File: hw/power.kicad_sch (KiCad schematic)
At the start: 6 parts, among them Q1 SI2301CDS-T1-GE3, U7 XC6206P332MR

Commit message: hw: add more information to BOM
Signed-off-by: Mahyar Koshkouei <mk@deltabeard.com>
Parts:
- C21, C22: MFr (none) -> CL10A105KB8NNNC; Manufacturer (none) -> Samsung Electro-Mechanics; Notes (none) -> Alternative manufacturer is acceptable
- D1: Manufacturer (none) -> Changjiang Electronics Tech (CJ)
- Q1: MFr (none) -> SI2301CDS-T1-GE3; Manufacturer (none) -> Vishay Intertech
- R8: MFr (none) -> 0603WAF1003T5E; Manufacturer (none) -> UNI-ROYAL(Uniroyal Elec); Notes (none) -> Alternative manufacturer is acceptable
- U7: MFr (none) -> XC6206P332MR; Manufacturer (none) -> Torex Semicon
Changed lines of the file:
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@@
+      (effects (font (size 1.27 1.27)) hide)
+    )
+    (property "Notes" "Alternative manufacturer is acceptable" (id 5) (at 116.84 102.87 0)
+      (effects (font (size 1.27 1.27)) hide)
+    )
+    (property "Description" " ±1% 100kΩ ±100ppm/℃ 0.1W 0603 Chip Resistor - Surface Mount ROHS " (id 6) (at 116.84 102.87 0)
+      (effects (font (size 1.27 1.27)) hide)
+    )
+    (property "MFr" "0603WAF1003T5E" (id 7) (at 116.84 102.87 0)
+      (effects (font (size 1.27 1.27)) hide)
+    )
+    (property "Manufacturer" " UNI-ROYAL(Uniroyal Elec) " (id 8) (at 116.84 102.87 0)
       (effects (font (size 1.27 1.27)) hide)
     )
@@
       (effects (font (size 1.27 1.27)) hide)
     )
+    (property "Description" " X5R ±10% 50V 1uF 0603 Multilayer Ceramic Capacitors MLCC - SMD/SMT ROHS " (id 5) (at 154.94 81.28 0)
+      (effects (font (size 1.27 1.27)) hide)
+    )
+    (property "MFr" "CL10A105KB8NNNC" (id 6) (at 154.94 81.28 0)
+      (effects (font (size 1.27 1.27)) hide)
+    )
+    (property "Manufacturer" " Samsung Electro-Mechanics " (id 7) (at 154.94 81.28 0)
+      (effects (font (size 1.27 1.27)) hide)
+    )
+    (property "Notes" "Alternative manufacturer is acceptable" (id 8) (at 154.94 81.28 0)
+      (effects (font (size 1.27 1.27)) hide)
+    )
     (pin "1")
     (pin "2")
@@
       (effects (font (size 1.27 1.27)) hide)
     )
+    (property "Description" " X5R ±10% 50V 1uF 0603 Multilayer Ceramic Capacitors MLCC - SMD/SMT ROHS " (id 5) (at 181.61 81.28 0)
+      (effects (font (size 1.27 1.27)) hide)
+    )
+    (property "MFr" "CL10A105KB8NNNC" (id 6) (at 181.61 81.28 0)
+      (effects (font (size 1.27 1.27)) hide)
+    )
+    (property "Manufacturer" " Samsung Electro-Mechanics " (id 7) (at 181.61 81.28 0)
+      (effects (font (size 1.27 1.27)) hide)
+    )
+    (property "Notes" "Alternative manufacturer is acceptable" (id 8) (at 181.61 81.28 0)
+      (effects (font (size 1.27 1.27)) hide)
+    )
     (pin "1")
     (pin "2")
@@
     )
     (property "MFr" "BAV70" (id 5) (at 139.7 77.47 0)
+      (effects (font (size 1.27 1.27)) hide)
+    )
+    (property "Description" " +150℃ (Tj) 225mW 6ns 1.25V 150mA 200mA Dual Common Cathode 70V 2.5uA 70V SOT-23 Switching Diode ROHS " (id 6) (at 139.7 77.47 0)
+      (effects (font (size 1.27 1.27)) hide)
+    )
+    (property "Manufacturer" " Changjiang Electronics Tech (CJ) " (id 7) (at 139.7 77.47 0)
       (effects (font (size 1.27 1.27)) hide)
     )
@@
       (effects (font (size 1.27 1.27)) hide)
     )
+    (property "Description" " +150℃ (Tj) 225mW 6ns 1.25V 150mA 200mA Dual Common Cathode 70V 2.5uA 70V SOT-23 Switching Diode ROHS " (id 6) (at 139.7 88.9 0)
+      (effects (font (size 1.27 1.27)) hide)
+    )
+    (property "Manufacturer" " Changjiang Electronics Tech (CJ) " (id 7) (at 139.7 88.9 0)
+      (effects (font (size 1.27 1.27)) hide)
+    )
     (pin "2")
   )
@@
     )
     (property "LCSC" "C10487" (id 4) (at 124.46 91.44 0)
+      (effects (font (size 1.27 1.27)) hide)
+    )
+    (property "Description" " 0.112Ω 2.8A,4.5V 1V 250uA 3.1A 0.86W 20V P Channel SOT-23(SOT-23-3) MOSFETs ROHS " (id 5) (at 124.46 91.44 0)
+      (effects (font (size 1.27 1.27)) hide)
+    )
+    (property "MFr" "SI2301CDS-T1-GE3" (id 6) (at 124.46 91.44 0)
+      (effects (font (size 1.27 1.27)) hide)
+    )
+    (property "Manufacturer" " Vishay Intertech " (id 7) (at 124.46 91.44 0)
       (effects (font (size 1.27 1.27)) hide)
     )
@@
       (effects (font (size 1.27 1.27)) hide)
     )
+    (property "MFr" "XC6206P332MR" (id 5) (at 170.18 77.47 0)
+      (effects (font (size 1.27 1.27)) hide)
+    )
+    (property "Notes" "" (id 6) (at 170.18 77.47 0)
+      (effects (font (size 1.27 1.27)) hide)
+    )
+    (property "Manufacturer" "Torex Semicon" (id 7) (at 170.18 77.47 0)
+      (effects (font (size 1.27 1.27)) hide)
+    )
+    (property "Description" " 6V 680mV @ 100mA Fixed 3.3V SOT-23-3L Linear Voltage Regulators (LDO) ROHS " (id 8) (at 170.18 77.47 0)
+      (effects (font (size 1.27 1.27)) hide)
+    )

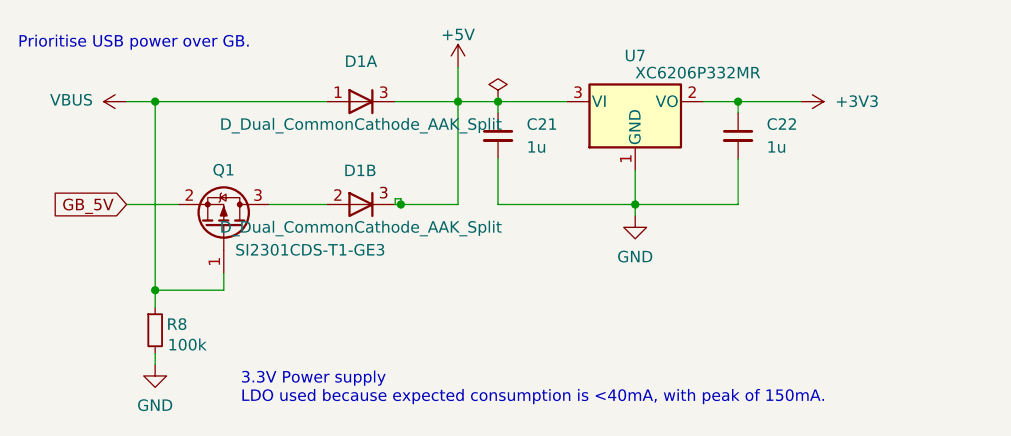
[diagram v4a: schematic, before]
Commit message: hw: fix USB
Additionally reduced the size of the battery holder.

Signed-off-by: Mahyar Koshkouei <mk@deltabeard.com>
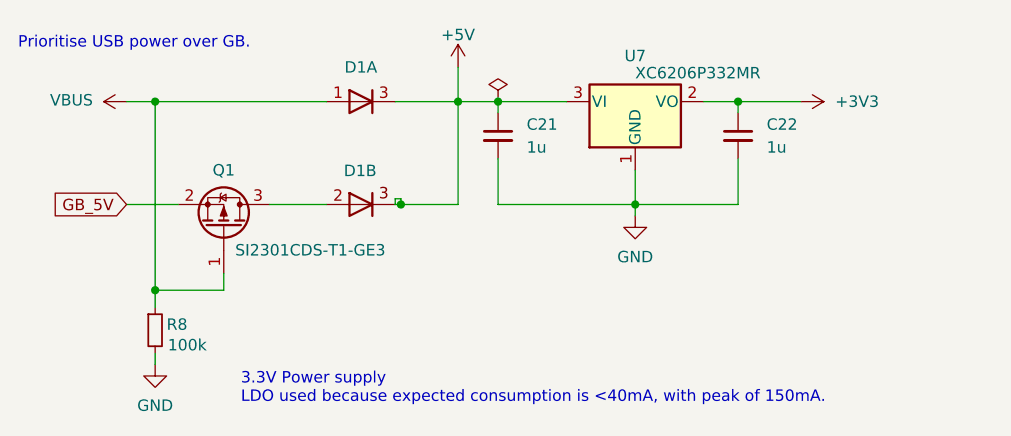
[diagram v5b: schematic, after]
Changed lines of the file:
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@@
   (symbol (lib_id "Device:D_Dual_CommonCathode_AAK_Split") (at 139.7 77.47 0) (unit 1)
     (in_bom yes) (on_board yes) (fields_autoplaced)
-    (property "Reference" "D1" (id 0) (at 139.7 73.025 0))
-    (property "Value" "D_Dual_CommonCathode_AAK_Split" (id 1) (at 139.7 80.01 0))
+    (property "Reference" "D1" (id 0) (at 139.7 73.66 0))
+    (property "Value" "D_Dual_CommonCathode_AAK_Split" (id 1) (at 139.7 80.01 0)
+      (effects (font (size 1.27 1.27)) hide)
+    )
     (property "Footprint" "Package_TO_SOT_SMD:SOT-23" (id 2) (at 137.16 80.01 0)
       (effects (font (size 1.27 1.27)) hide)
@@
       (effects (font (size 1.27 1.27)) (justify left))
     )
-    (property "Value" "D_Dual_CommonCathode_AAK_Split" (id 1) (at 139.7 91.44 0))
+    (property "Value" "D_Dual_CommonCathode_AAK_Split" (id 1) (at 139.7 91.44 0)
+      (effects (font (size 1.27 1.27)) hide)
+    )
     (property "Footprint" "Package_TO_SOT_SMD:SOT-23" (id 2) (at 137.16 91.44 0)
       (effects (font (size 1.27 1.27)) hide)

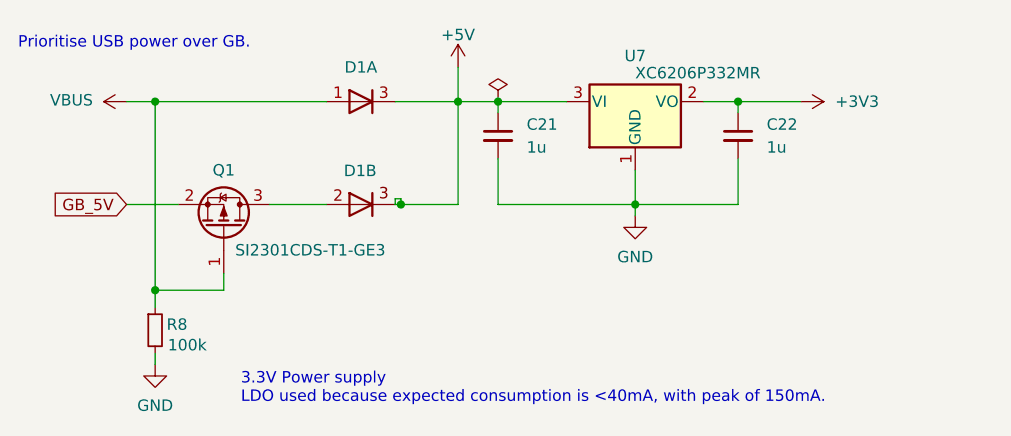
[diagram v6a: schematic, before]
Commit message: hw: use nets for decoupling capacitors
Signed-off-by: Mahyar Koshkouei <mk@deltabeard.com>
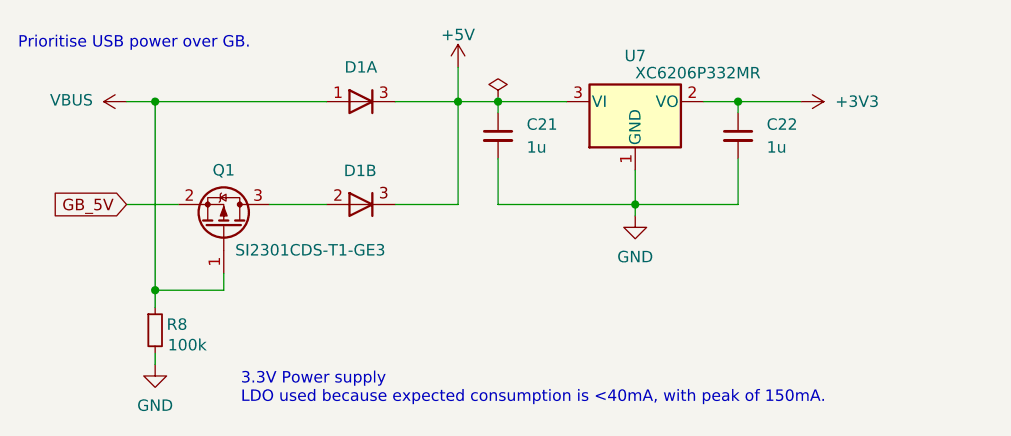
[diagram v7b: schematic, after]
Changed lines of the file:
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@@
   (junction (at 116.84 77.47) (diameter 0.9144) (color 0 0 0 0))
   (junction (at 116.84 98.425) (diameter 0.9144) (color 0 0 0 0))
-  (junction (at 144.145 88.9) (diameter 0.9144) (color 0 0 0 0))
   (junction (at 150.495 77.47) (diameter 0.9144) (color 0 0 0 0))
   (junction (at 154.94 77.47) (diameter 0.9144) (color 0 0 0 0))
@@
     (stroke (width 0) (type solid) (color 0 0 0 0))
   )
-  (wire (pts (xy 143.51 88.265) (xy 144.145 88.265))
-    (stroke (width 0) (type solid) (color 0 0 0 0))
-  )
-  (wire (pts (xy 143.51 88.9) (xy 143.51 88.265))
-    (stroke (width 0) (type solid) (color 0 0 0 0))
-  )
-  (wire (pts (xy 143.51 88.9) (xy 144.145 88.9))
-    (stroke (width 0) (type solid) (color 0 0 0 0))
-  )
-  (wire (pts (xy 144.145 88.265) (xy 144.145 88.9))
-    (stroke (width 0) (type solid) (color 0 0 0 0))
-  )
-  (wire (pts (xy 144.145 88.9) (xy 150.495 88.9))
-    (stroke (width 0) (type solid) (color 0 0 0 0))
-  )
   (wire (pts (xy 150.495 73.66) (xy 150.495 77.47))
     (stroke (width 0) (type solid) (color 0 0 0 0))
@@
     (stroke (width 0) (type solid) (color 0 0 0 0))
   )
+  (wire (pts (xy 150.495 88.9) (xy 143.51 88.9))
+    (stroke (width 0) (type default) (color 0 0 0 0))
+  )
   (wire (pts (xy 150.495 88.9) (xy 150.495 77.47))

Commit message: all: Add open source license
Signed-off-by: Mahyar Koshkouei <mk@deltabeard.com>
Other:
- company: Mahyar Koshkouei -> Copyright (c) 2021 Mahyar Koshkouei
- title: RP2040 Game Boy Cart -> DBGC: RP2040 Game Boy Cart
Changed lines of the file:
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@@
   (paper "A4")
   (title_block
-    (title "RP2040 Game Boy Cart")
+    (title "DBGC: RP2040 Game Boy Cart")
     (date "2021-09-29")
     (rev "0.3a")
-    (company "Mahyar Koshkouei")
-    (comment 1 "All Rights Reserved")
+    (company "Copyright (c) 2021 Mahyar Koshkouei")
+    (comment 1 "CC BY-SA 4.0")
     (comment 2 "Compatible with DMG, MGB, & CGB. Collectively referred to as \"GB\" here.")
   )
